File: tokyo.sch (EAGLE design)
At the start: 52 parts, among them J1 254-2X5F, J2 254-2X5M, P1 9774050151, P2 9774050151, P3 9774050151, P4 9774050151, Q1 STD6N95K5, T1 750313823, U1 UCC28710, X1 508-1X3B

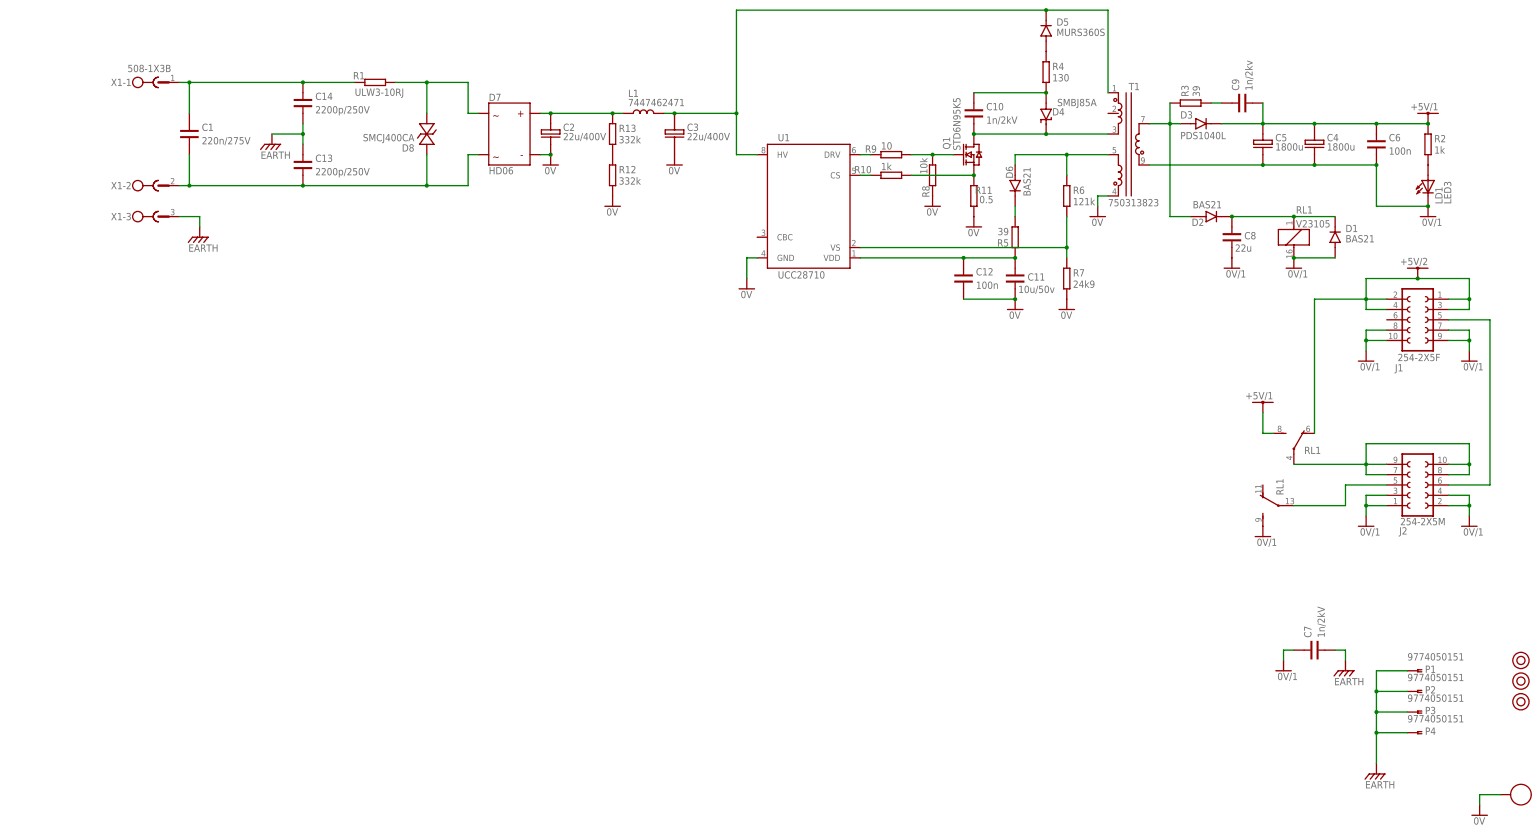
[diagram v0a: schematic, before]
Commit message: Removed relais, added choke, added dissipation area for output diode, added minimum load circuiRemoved relais, added choke, added dissipation area for output diode, added minimum load circuit.
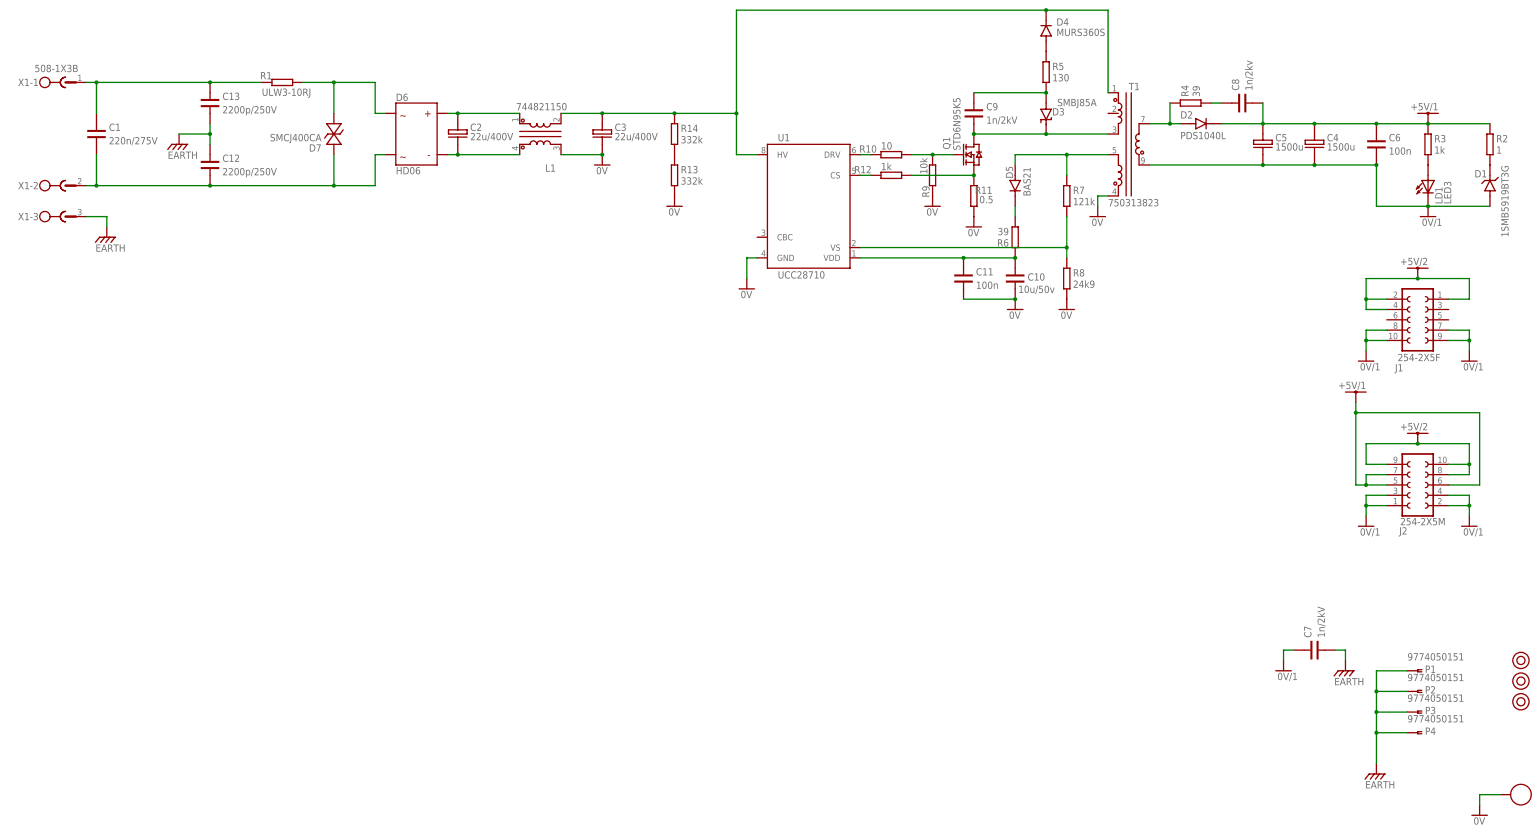
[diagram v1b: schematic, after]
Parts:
- removed C14: 2200p/250V, capacitors:C2211
- removed D8: SMCJ400CA, supressors:SMCJ400CA
- removed RL1: V23105, relais:V23105
- added R14: 332k, resistors:R1206
- C10: value 1n/2kV -> 10u/50v; device capacitors:C1812 -> capacitors:C1206
- C11: value 10u/50v -> 100n; device capacitors:C1206 -> capacitors:C0603
- C12: value 100n -> 2200p/250V; device capacitors:C0603 -> capacitors:C2211
- C4, C5: value 1800u -> 1500u; device capacitors:C+D13 -> capacitors:C+D10
- C8: value 22u -> 1n/2kv; device capacitors:C1206 -> capacitors:C1812
- C9: value 1n/2kv -> 1n/2kV
- D1: value BAS21 -> 1SMB5919BT3G; device diodes:BAS21 -> diodes:1SMB59XXBT3G
- D2: value BAS21 -> PDS1040L; device diodes:BAS21 -> diodes:PDS1040L
- D3: value PDS1040L -> SMBJ85A; device diodes:PDS1040L -> supressors:SMBJ85A
- D4: value SMBJ85A -> MURS360S; device supressors:SMBJ85A -> diodes:MURS360S
- D5: value MURS360S -> BAS21; device diodes:MURS360S -> diodes:BAS21
- D6: value BAS21 -> HD06; device diodes:BAS21 -> diodes:HD06
- D7: value HD06 -> SMCJ400CA; device diodes:HD06 -> supressors:SMCJ400CA
- L1: value 7447462471 -> 744821150; device powermagnetics:7447462471 -> powermagnetics:744821150
- R10: value 1k -> 10
- R12: value 332k -> 1k; device resistors:R1206 -> resistors:R0603
- R2: value 1k -> 1; device resistors:R0603 -> resistors:R1206
- R3: value 39 -> 1k; device resistors:R1206 -> resistors:R0603
- R4: value 130 -> 39
- R5: value 39 -> 130; device resistors:R0603 -> resistors:R1206
- R6: value 121k -> 39
- R7: value 24k9 -> 121k
- R8: value 10k -> 24k9
- R9: value 10 -> 10k
- renumbered TP1 to 0V
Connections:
- removed net N$19: J2.10, J2.7, J2.8, J2.9, RL1G$3.P
- removed net N$22: J1.5, J2.6
- removed net N$27: C8.1, D1.1, D2.1, RL1G$1.1
- new net N$20: C2.2, D6.2, L1.4
- net +5V/1: now also C8.2, D2.1, J2.5, J2.6, J2.7, R3.1; no longer C9.2, D3.1, RL1G$3.S
- net +5V/2: now also J2.10, J2.8, J2.9; no longer J1.3, RL1G$3.O
- net 0V: now also C10.2, L1.3, R13.2, R8.2, R9.1; no longer C12.2, C2.2, D7.2, R12.2, R7.2, R8.1
- net 0V/1: no longer C8.2, RL1G$1.2, RL1G$2.S
- net EARTH: now also C12.1, C13.2; no longer C13.1, C14.2
- net N$1: now also C13.1; no longer C14.1
- net N$10: now also D4.2, R5.1; no longer D5.2, R4.1
- net N$11: now also C9.2, D3.C; no longer C10.2, D4.C
- net N$12: now also R12.2; no longer R10.2
- net N$13: now also R12.1; no longer R10.1
- net N$14: now also R10.2; no longer R8.2
- net N$15: now also C10.1, R6.1; no longer C12.1, R5.1
- net N$16: now also D1.1, R2.2; no longer R12.1, R13.2
- net N$17: now also C9.1, D3.A, R5.2; no longer C10.1, D4.A, R4.2
- net N$18: now also R7.2, R8.1; no longer R6.2, R7.1
- net N$2: now also C12.2, D6.4, D7.P$1; no longer C13.2, D7.4, D8.P$1
- net N$21: now also C2.1, D6.1, L1.1; no longer J2.5, RL1G$2.P
- net N$23: now also R10.1; no longer R9.1
- net N$26: now also D5.1, R6.2; no longer D6.1, R5.2
- net N$3: now also D5.2, R7.1; no longer D6.2, R6.1
- net N$4: now also D6.3, D7.P$2; no longer D7.3, D8.P$2
- net N$5: now also R3.2; no longer R2.2
- net N$6: now also C8.1, R4.2; no longer C9.1, R3.2
- net N$7: now also R14.2; no longer C2.1, D7.1, L1.1
- net N$8: now also R4.1; no longer D3.2, R3.1
- net N$9: now also D4.1, R14.1; no longer D5.1
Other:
- moved on the sheet: C1, C10, C11, C12, C13, C2, C3, C8, C9, D2, D5, R1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

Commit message: Revision for manufacturing.
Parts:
- C1: value 220n/275V -> 220n/275Vac; device capacitors:C13X8 -> capacitors:C14X8
- C12, C13: value 2200p/250V -> 2200p/250Vac
- C7, C9: value 1n/2kV -> 1000p/250Vac
- C8: value 1n/2kv -> 1000p/250Vac
- D1: device diodes:1SMB59XXBT3G -> diodes:1SMB5919BT3G
- R11: value 0.5 -> 0.5/0.8W
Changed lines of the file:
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@@
 <part name="FRAME1" library="frames" deviceset="A3LANDSCAPE" device=""/>
 <part name="X1" library="board-to-wire" deviceset="508-1X3B" device=""/>
-<part name="C1" library="capacitors" deviceset="C" device="13X8" value="220n/275V"/>
-<part name="C12" library="capacitors" deviceset="C" device="2211" value="2200p/250V"/>
-<part name="C13" library="capacitors" deviceset="C" device="2211" value="2200p/250V"/>
+<part name="C1" library="capacitors" deviceset="C" device="14X8" value="220n/275Vac"/>
+<part name="C12" library="capacitors" deviceset="C" device="2211" value="2200p/250Vac"/>
+<part name="C13" library="capacitors" deviceset="C" device="2211" value="2200p/250Vac"/>
 <part name="R1" library="resistors" deviceset="R" device="15X6" value="ULW3-10RJ"/>
 <part name="D7" library="supressors" deviceset="SMCJ400CA" device=""/>
@@
 <part name="FIDUCIAL3" library="unsorted" deviceset="FIDUCIAL" device=""/>
 <part name="FIDUCIAL1" library="unsorted" deviceset="FIDUCIAL" device=""/>
-<part name="C7" library="capacitors" deviceset="C" device="1812" value="1n/2kV"/>
+<part name="C7" library="capacitors" deviceset="C" device="1812" value="1000p/250Vac"/>
 <part name="SUPPLY1" library="powersymbols" deviceset="EARTH" device=""/>
 <part name="SUPPLY2" library="powersymbols" deviceset="EARTH" device=""/>
@@
 <part name="D4" library="diodes" deviceset="MURS360S" device=""/>
 <part name="R5" library="resistors" deviceset="R" device="1206" value="130"/>
-<part name="C9" library="capacitors" deviceset="C" device="1812" value="1n/2kV"/>
+<part name="C9" library="capacitors" deviceset="C" device="1812" value="1000p/250Vac"/>
 <part name="U1" library="integratedcircuits" deviceset="UCC28710" device=""/>
 <part name="D5" library="diodes" deviceset="BAS21" device=""/>
@@
 <part name="R8" library="resistors" deviceset="R" device="0603" value="24k9"/>
 <part name="R12" library="resistors" deviceset="R" device="0603" value="1k"/>
-<part name="R11" library="resistors" deviceset="R" device="2512" value="0.5"/>
+<part name="R11" library="resistors" deviceset="R" device="2512" value="0.5/0.8W"/>
 <part name="C6" library="capacitors" deviceset="C" device="0603" value="100n"/>
 <part name="R3" library="resistors" deviceset="R" device="0603" value="1k"/>
@@
 <part name="C5" library="capacitors" deviceset="C+" device="D10" value="1500u"/>
 <part name="J2" library="board-to-board" deviceset="254-2X5M" device="" value="254-2X5M"/>
-<part name="C8" library="capacitors" deviceset="C" device="1812" value="1n/2kv"/>
+<part name="C8" library="capacitors" deviceset="C" device="1812" value="1000p/250Vac"/>
 <part name="J1" library="board-to-board" deviceset="254-2X5F" device="" value="254-2X5F"/>
 <part name="D2" library="diodes" deviceset="PDS1040L" device=""/>
@@
 <part name="0V7" library="powersymbols" deviceset="0V" device=""/>
 <part name="U$7" library="powersymbols" deviceset="+5V/2" device=""/>
-<part name="D1" library="diodes" deviceset="1SMB59XXBT3G" device="" value="1SMB5919BT3G"/>
+<part name="D1" library="diodes" deviceset="1SMB5919BT3G" device="" value="1SMB5919BT3G"/>
 <part name="R2" library="resistors" deviceset="R" device="1206" value="1"/>
 </parts>
@@
 </instance>
 <instance part="R11" gate="A" x="241.3" y="190.5" smashed="yes" rot="R180">
-<attribute name="NAME" x="245.872" y="192.786" size="1.778" layer="95" ratio="10" rot="R180"/>
-<attribute name="VALUE" x="246.126" y="188.722" size="1.778" layer="96" ratio="10" rot="R180" align="top-left"/>
+<attribute name="NAME" x="238.252" y="190.246" size="1.778" layer="95" ratio="10" rot="R270"/>
+<attribute name="VALUE" x="244.348" y="196.596" size="1.778" layer="96" ratio="10" rot="R270" align="top-left"/>
 </instance>
 <instance part="C6" gate="G$1" x="340.36" y="203.2" smashed="yes">
